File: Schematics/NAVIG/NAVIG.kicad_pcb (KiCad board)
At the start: 4 copper layers, 78 x 78 mm, 70 parts, among them J1 GNSS_SMA, J2 SWD, J3 USART, J4 3.3V IN, J5 CNTRL I2C, J6 USB_C_Receptacle_USB2.0, SW1 Omron_B3F-10xx, SW2 Omron_B3F-10xx, U1 BMP390, U2 BNO055, U3 NEO-M9N, U4 STM32F205RETx, U6 USBLC6-2SC6, Y1 32.768KHz, Y2 12MHz_ECS-120-18-33-JGN-TR3, Y3 32.768KHz_SC32S-7PF20PPM

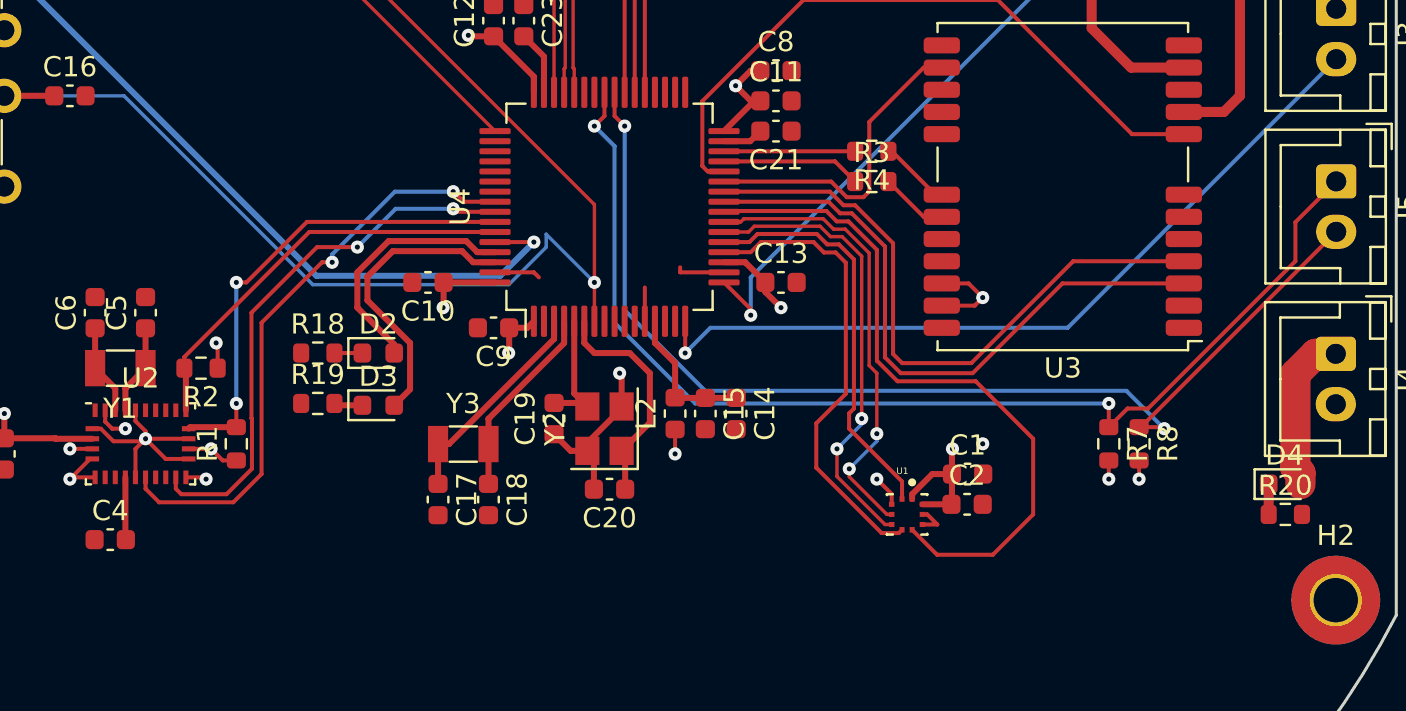
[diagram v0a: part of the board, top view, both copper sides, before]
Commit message: NAVIG v1 fixes and some experimental CNTRL updates for v2
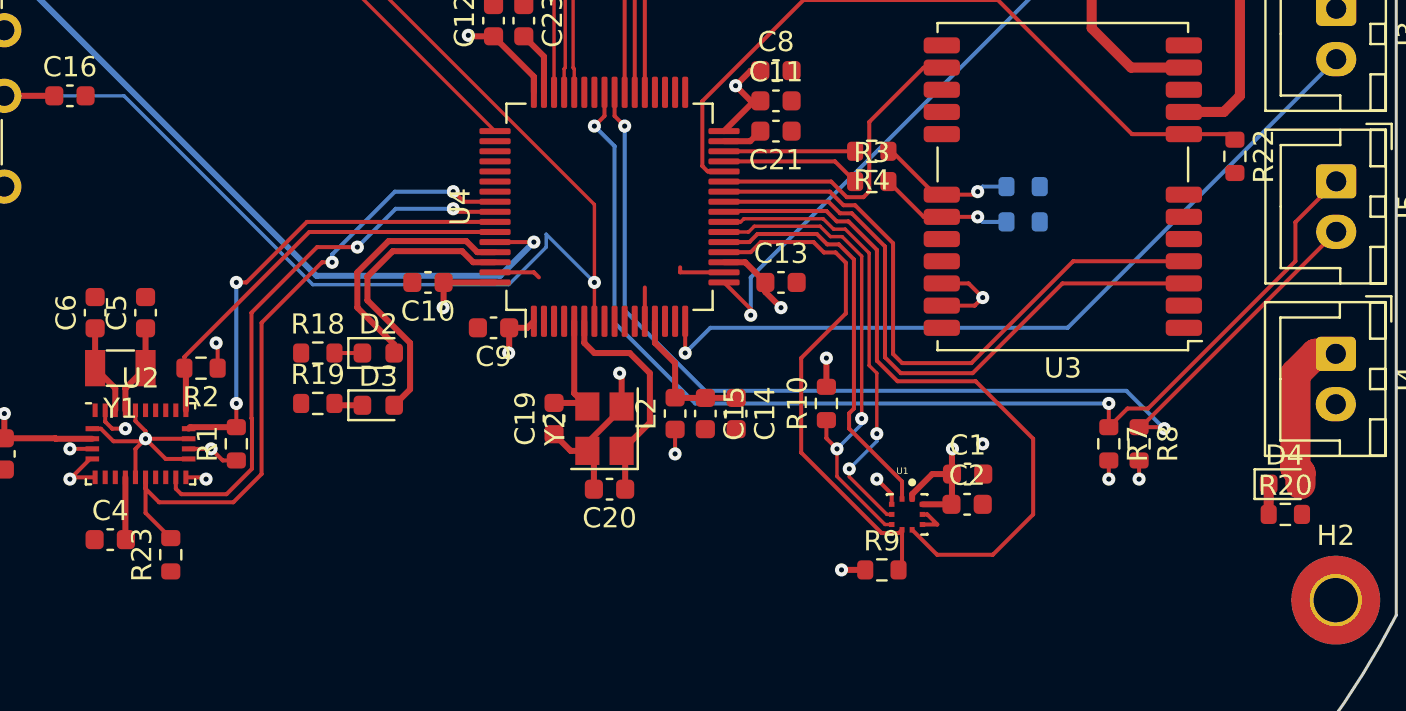
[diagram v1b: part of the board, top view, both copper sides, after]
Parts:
- removed C17, C18: 22pF, Capacitor_SMD:C_0603_1608Metric
- removed Y3: 32.768KHz_SC32S-7PF20PPM, Crystal:Crystal_SMD_3215-2Pin_3.2x1.5mm
- added R10: 10K, Resistor_SMD:R_0603_1608Metric, F.Cu at (161.0, 101.2)
- added R13: 4.7K, Resistor_SMD:R_0603_1608Metric, B.Cu at (170.8, 90.5)
- added R21: 4.7K, Resistor_SMD:R_0603_1608Metric, B.Cu at (170.8, 92.2)
- added R22: 10K, Resistor_SMD:R_0603_1608Metric, F.Cu at (181.2, 89.0)
- added R23: 10K, Resistor_SMD:R_0603_1608Metric, F.Cu at (128.5, 108.8)
- added R9: 10K, Resistor_SMD:R_0603_1608Metric, F.Cu at (163.8, 109.5)
- R1, R2: value 10K -> 4.7K
- R7, R8: value 1K -> 4.7K
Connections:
- U4 pad 3: LSE_IN -> unconnected-(U4-PC14-Pad3)
- U4 pad 4: LSE_OUT -> unconnected-(U4-PC15-Pad4)
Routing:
- net LSE_IN: track 10.8 -> 0.00 mm
- net LSE_OUT: track 9.62 -> 0.00 mm
- net IMU_RESET: track 29.4 -> 32.9 mm
- net Net-(U3-SDA/~{SPI_CS}): track 3.54 -> 6.91 mm, vias 0 -> 1
- net Net-(U3-SCL/SPI_CLK): track 3.37 -> 6.68 mm, vias 0 -> 1
- net SPI1_CSB: track 23.1 -> 25.8 mm
- net GNSS_RESET: track 33.1 -> 35.7 mm
- net +3.3V: track 58.7 -> 61.3 mm, vias 17 -> 19
- net SPI1_MISO: track 22.7 -> 24.3 mm

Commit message: slight fixes to navig board for final production run
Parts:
- added J7: Reset Jumper, Connector_PinHeader_2.54mm:PinHeader_1x02_P2.54mm_Vertical, F.Cu at (123.8, 91.0)
- moved C19 7.31 mm to (145.4, 109.0)
- moved C20 7.31 mm to (148.2, 112.5)
- moved Y2 7.31 mm to (147.9, 109.5)
- moved C16 6.40 mm to (127.5, 91.0)
- moved C1 1.00 mm to (168.0, 103.8)
- moved R8 0.75 mm to (177.2, 103.2)
- moved R15 0.50 mm to (154.0, 70.8)
- moved R17 0.50 mm to (158.0, 70.8)
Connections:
- SW2 pad 1: SWD_NRST -> Net-(J7-Pin_2)
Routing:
- net SWD_NRST: track 72.8 -> 57.6 mm, vias 1 -> 2
- net Net-(J7-Pin_2): track 0.00 -> 11.0 mm
- net HSE_IN: track 6.22 -> 13.5 mm
- net HSE_OUT: track 11.3 -> 16.7 mm
- net +3.3V: track 61.3 -> 66.0 mm, vias 19 -> 20
- net GND: track 38.6 -> 42.6 mm
- net BOOT0: track 45.4 -> 43.3 mm
- net I2C3_SDA: track 55.3 -> 56.1 mm
- net I2C3_SCL: track 56.8 -> 56.1 mm

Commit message: final nav
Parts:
- added TP1: 3.3V, TestPoint:TestPoint_Pad_D2.0mm, F.Cu at (164.0, 77.2)
- R13, R21, U6: moved to F.Cu
- moved R13 13.9 mm to (177.8, 78.5)
- moved R21 13.9 mm to (177.8, 80.2)
- moved U6 6.52 mm to (144.0, 67.2)
- moved R11 2.85 mm to (149.8, 64.8)
- moved R12 1.75 mm to (145.8, 62.5), turned to 180 degrees
- moved C13 1.35 mm to (159.2, 96.5)
- moved C9 1.12 mm to (143.5, 98.0)
- moved C21 1.03 mm to (159.5, 87.5)
- moved C8 1.00 mm to (158.5, 83.8)
- moved C14 0.97 mm to (157.5, 101.8)
- moved C19 0.90 mm to (144.5, 109.0)
- moved C20 0.75 mm to (148.2, 113.2)
- moved C5 0.75 mm to (127.2, 96.0)
- moved C6 0.75 mm to (124.8, 96.0)
- moved R5 0.66 mm to (179.2, 73.8)
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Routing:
- net Net-(U3-SDA/~{SPI_CS}): track 6.91 -> 22.3 mm, vias 1 -> 2
- net Net-(U3-SCL/SPI_CLK): track 6.68 -> 21.1 mm, vias 1 -> 2
- net /USB_RAW_D-: track 7.81 -> 16.7 mm, vias 1 -> 2
- net VBUS: track 15.4 -> 22.4 mm, vias 1 -> 0
- net /USB_RAW_D+: track 7.18 -> 12.5 mm, vias 1 -> 2
- net +3.3V: track 66.0 -> 71.3 mm, vias 20 -> 21
- net /RF_GNSS_MATCH: track 6.69 -> 11.6 mm
- net Net-(J6-CC1): track 1.74 -> 4.72 mm
- net GNSS_RESET: track 35.7 -> 37.0 mm
- net Net-(J6-CC2): track 2.16 -> 3.37 mm
- net Net-(U4-VCAP_1): track 2.01 -> 3.11 mm
- net HSE_OUT: track 16.7 -> 17.7 mm
- net +3.3VA: track 7.23 -> 8.22 mm
- net SPI1_CSB: track 25.8 -> 24.8 mm
- net HSE_IN: track 13.5 -> 14.4 mm
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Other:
- board text added: "3.3V"
- board text added: "BOOT"
- board text added: "Designed By: Arav Sonawane February 2025"
- board text added: "ERROR"
- board text added: "I2C OUT"
- board text added: "LED"
- board text added: "NAVION NAVIGATION BOARD"
- board text added: "PWR"
- board text added: "REMOVE JUMPER FOR FLIGHT!"
- board text added: "RESET"
- board text added: "STATUS"
- board text added: "SWD"
- board text added: "USART"
- board text added: "v1.0"
